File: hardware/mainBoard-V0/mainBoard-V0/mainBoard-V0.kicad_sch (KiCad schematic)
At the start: 20 parts, among them SW1 SW_SPDT, U1 STM32WB55CCU6ND, Y1 ABM12W-32.0MHZ, Y3 ABS07-32.768KHZ

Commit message: Added net labels and assets.
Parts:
- added C15: 4.7u, symbol Device:C
- added E1: AMCA31-2R450G-S1F-T3, AMCA31-2R450G-S1F-T3:XDCR_AMCA31-2R450G-S1F-T3, symbol AMCA31-2R450G-S1F-T3:AMCA31-2R450G-S1F-T3
- added J1: B5B-XH-A, B5B-XH-A:JST_B5B-XH-A, symbol B5B-XH-A:B5B-XH-A
- added L1: 10n, symbol Device:L
- added L2: 10u, symbol Device:L
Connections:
- net GND: now also C15.1
- net SPI1_SCK: now reaches U1.10 (PA1)
- net SPI1_MISO: now reaches U1.15 (PA6)
- net SPI1_MOSI: now reaches U1.16 (PA7)
- net USART1_TX: now reaches U1.18 (PA9)
- net at U1.31 (VFBSMPS): now also C15.2, L2.2
- net at U1.33 (VLXSMPS): now also L1.1
- net USART1_RX: now reaches U1.36 (PA10)
- net USB_DM: now reaches U1.37 (PA11)
- net USB_DP: now reaches U1.38 (PA12)
- new net: L1.2, L2.1
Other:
- moved on the sheet: C5, C6, Y1, Y3

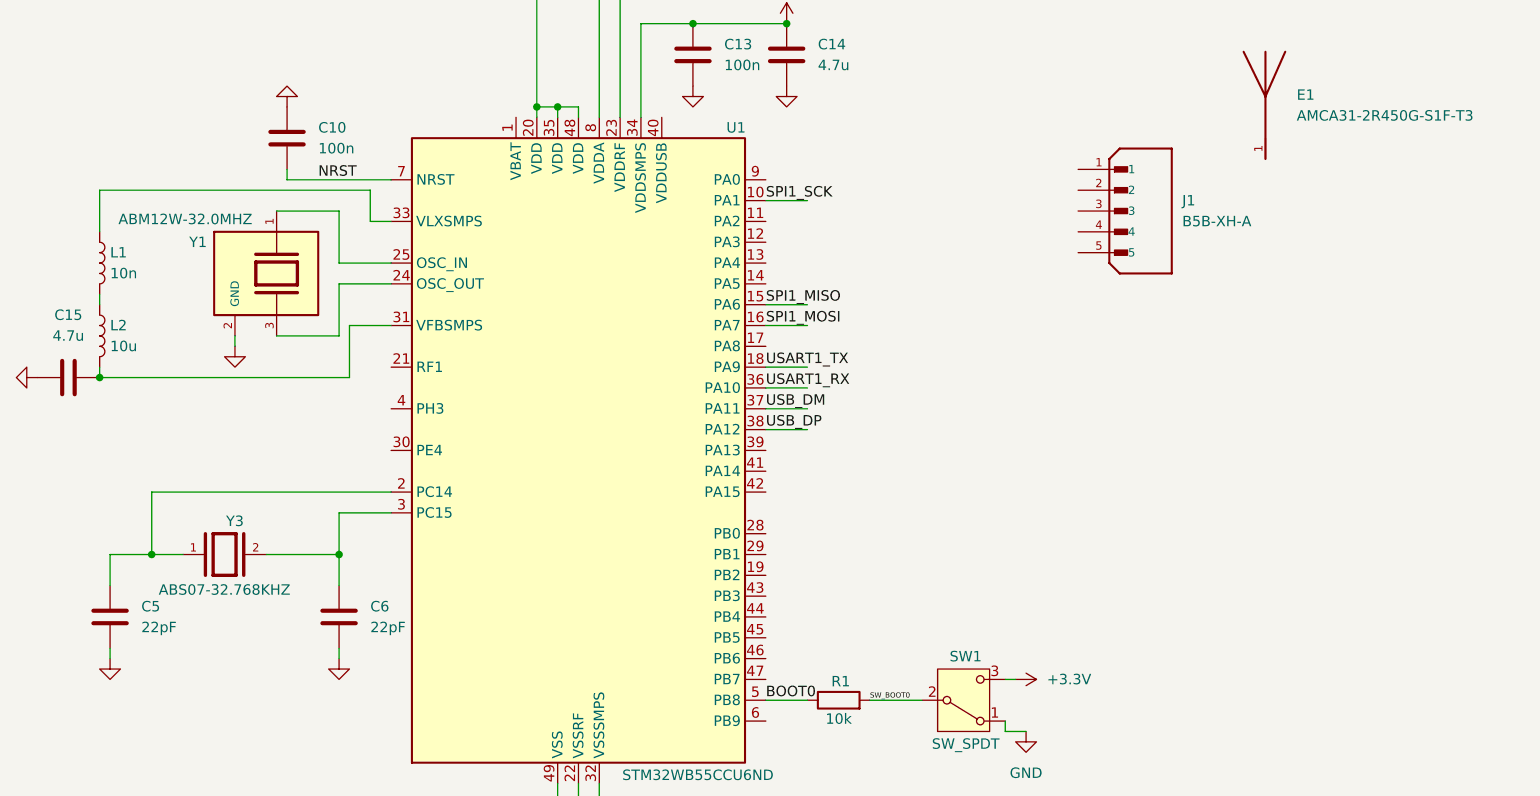
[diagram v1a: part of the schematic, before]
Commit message: Added more components to libraries
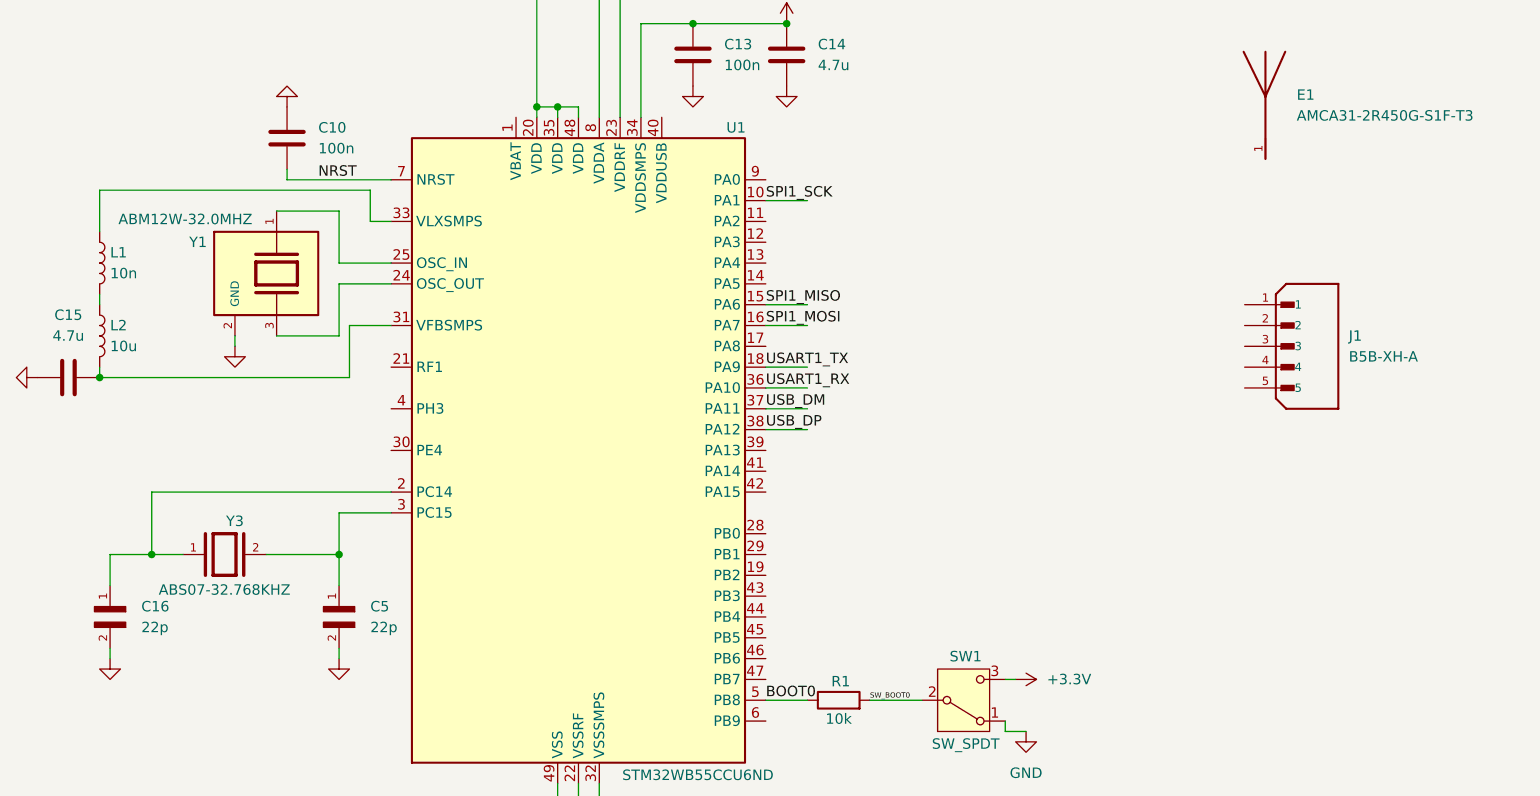
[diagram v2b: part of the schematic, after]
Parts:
- removed C5, C6: 22pF, symbol Device:C
- added C16, C5: 22p, CC0402FRNPO9BN220:CAPC1005X55N, symbol CC0402FRNPO9BN220:CC0402FRNPO9BN220
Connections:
- net GND: now also C16.2, C5.2
- net at U1.3 (PC15), Y3.2: now also C5.1
- net at U1.2 (PC14), Y3.1: now also C16.1
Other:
- moved on the sheet: J1

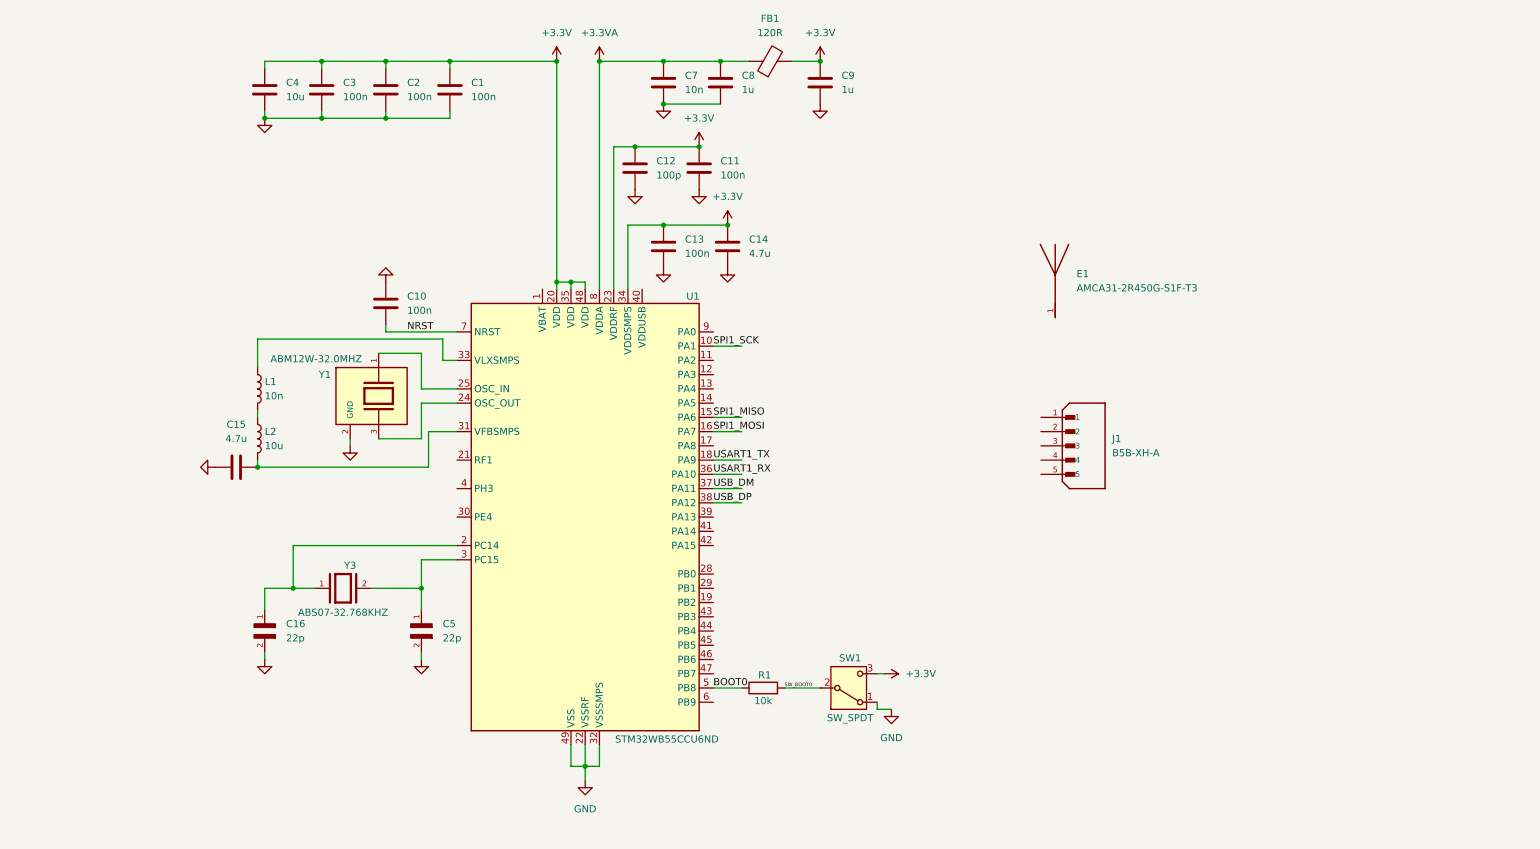
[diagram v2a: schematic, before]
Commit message: Added SWD header, type-c connector, RF antenna circuit, and battery charger with 3v3 regulator for power rail to schematic | Imported real component symbols and datasheets
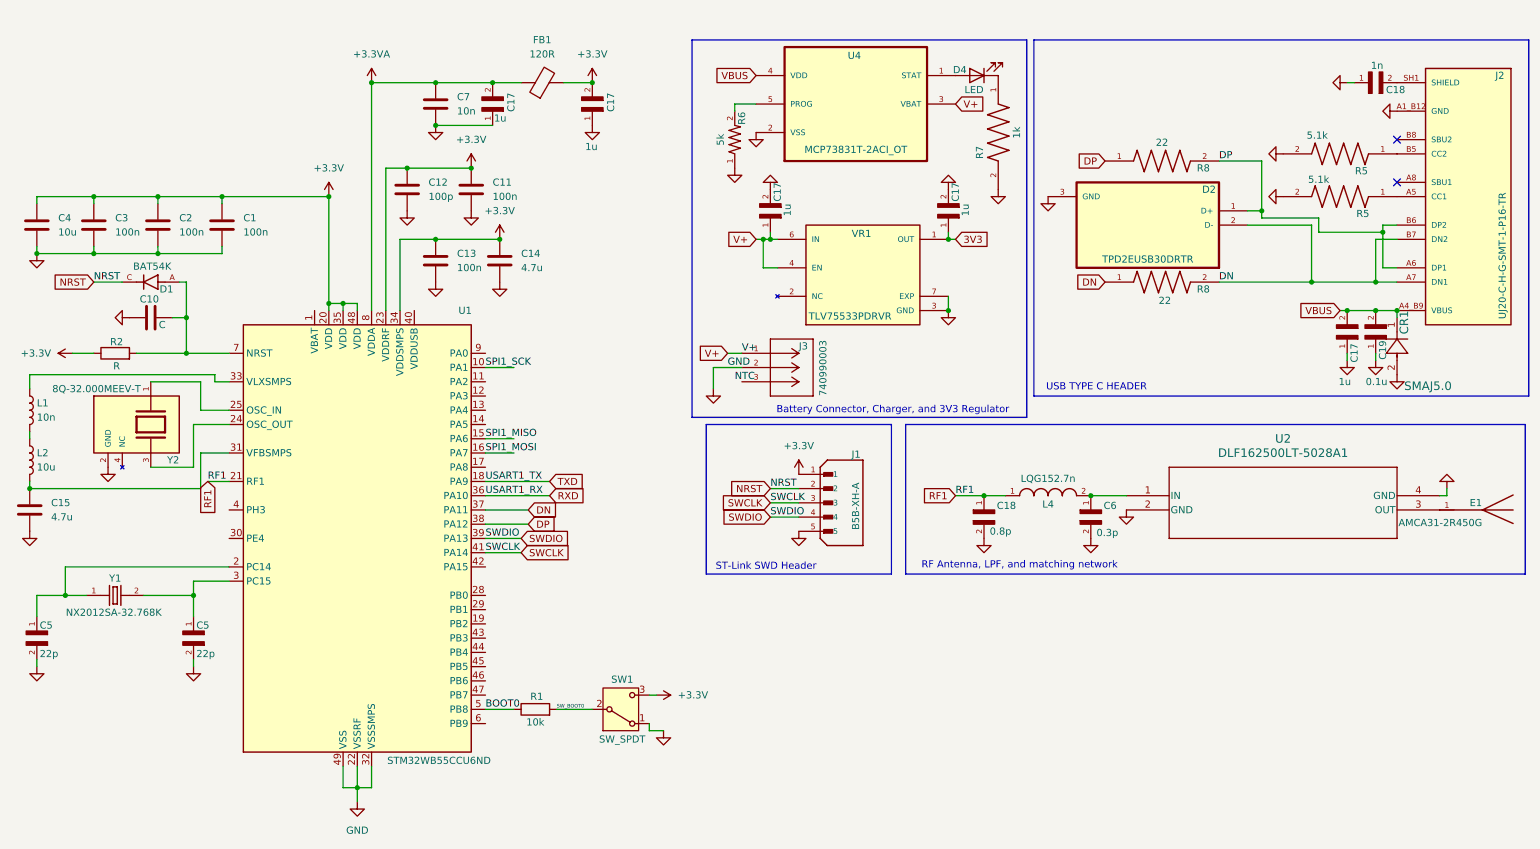
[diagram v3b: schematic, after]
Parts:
- removed C8, C9: 1u, symbol Device:C
- removed Y1: ABM12W-32.0MHZ, ABM12W-32.0000MHZ-6-D1X-T3:XTAL_ABM12W-32.0000MHZ-6-D1X-T3, symbol ABM12W-32.0000MHZ-6-D1X-T3:ABM12W-32.0000MHZ-6-D1X-T3
- removed Y3: ABS07-32.768KHZ, ABS07-32.768KHZ-T:XTAL_ABS07-32.768KHZ-T, symbol ABS07-32.768KHZ-T:ABS07-32.768KHZ-T
- added C17 (x5): 1u, JMK105BJ105KV-F:CAPC1005X55N, symbol JMK105BJ105KV-F:JMK105BJ105KV-F
- added C18: 0.8p, GRM1555C1HR80BA01D:CAPC1005X55N, symbol GRM1555C1HR80BA01D:GRM1555C1HR80BA01D
- added C18: 1n, GRM155R71H102KA01D:CAPC1005X55N, symbol GRM155R71H102KA01D:GRM155R71H102KA01D
- added C19: 0.1u, CL05A104KA5NNNC:CAPC1005X55N, symbol CL05A104KA5NNNC:CL05A104KA5NNNC
- added C6: 0.3p, GRM1555C1HR30WA01D:CAPC1005X55N, symbol GRM1555C1HR30WA01D:GRM1555C1HR30WA01D
- added CR1: SMAJ5.0, SMAJ5-0:SMASeries_LTF, symbol SMAJ5-0:SMAJ5.0
- added D1: BAT54K, BAT54KFILM:SODFL1608X70N, symbol BAT54KFILM:BAT54KFILM
- added D2: TPD2EUSB30DRTR, TPD2EUSB30DRTR:SOTFL35P100X50-3N, symbol TPD2EUSB30DRTR:TPD2EUSB30DRTR
- added D4: LED, symbol Device:LED
- added J2: UJ20-C-H-G-SMT-1-P16-TR, UJ20-C-H-G-SMT-1-P16-TR:SAMESKY_UJ20-C-H-G-SMT-1-P16-TR, symbol UJ20-C-H-G-SMT-1-P16-TR:UJ20-C-H-G-SMT-1-P16-TR
- added J3: 740990003, 740990003:CONN_SD-74099-001_03_MOL, symbol 740990003:740990003
- added L4: LQG152.7n, LQG15HS2N7S02D:INDC1005X55N, symbol LQG15HS2N7S02D:LQG15HS2N7S02D
- added R2: R, symbol Device:R
- added R5 (x2): 5.1k, CRCW04025K10FKED:RESC1005X40N, symbol CRCW04025K10FKED:CRCW04025K10FKED
- added R6: 5k, PNM0402E5001BST1:RESC1005X40, symbol PNM0402E5001BST1:PNM0402E5001BST1
- added R7: 1k, CRCW04021K00FKED:RESC1005X40N, symbol CRCW04021K00FKED:CRCW04021K00FKED
- added R8 (x2): 22, CRCW040222R0FKED:RESC1005X40N, symbol CRCW040222R0FKED:CRCW040222R0FKED
- added U2: DLF162500LT-5028A1, DLF-4_1P6X0P8, symbol 2026-02-12_05-16-45:DLF162500LT-5028A1
- added U4: MCP73831T-2ACI_OT, MCP73831T-2ACI_OT:SOT95P280X145-5N, symbol MCP73831T-2ACI_OT:MCP73831T-2ACI_OT
- added VR1: TLV75533PDRVR, TLV75533PDRVR:VREG_TLV75533PDRVR, symbol TLV75533PDRVR:TLV75533PDRVR
- added Y1: NX2012SA-32.768K, NX2012SA-32.768K-STD-MUB-1:XTAL_NX2012SA-32.768K-STD-MUB-1, symbol NX2012SA-32.768K-STD-MUB-1:NX2012SA-32.768K-STD-MUB-1
- added Y2: 8Q-32.000MEEV-T, 8Q-32.000MEEV-T:XTAL_8Q-32.000MEEV-T, symbol 8Q-32.000MEEV-T:8Q-32.000MEEV-T
- C10: value 100n -> C
- E1: value AMCA31-2R450G-S1F-T3 -> AMCA31-2R450G
- renumbered C16 to C5
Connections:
- net +3.3V: now also J1.1, C17.2, R2.1
- net +3.3VA: now also C17.2
- net GND: now also J1.5, C17.1, C17.1, C17.1, C17.2, C17.2, C18.1, C18.2, C19.1, C6.2, CR1.2, D2.3 (GND), J2.A1_B12 (GND), J2.B1_A12 (GND), J3.2, R5.2, R5.2, R6.1, R7.2, U2.2 (GND), U2.4 (GND), U4.2 (VSS), VR1.3 (GND), VR1.7 (EXP), Y2.2 (GND)
- net NRST: now also J1.2, D1.C; no longer C10.2, U1.7 (NRST)
- net SWCLK: now reaches J1.3
- net SWCLK: now also U1.41 (PA14)
- net SWDIO: now reaches J1.4
- net SWDIO: now also U1.39 (PA13)
- net at C5.1, U1.2 (PC14): now also Y1.1
- net RF1: now reaches U1.21 (RF1)
- net RF1: now also C18.1, L4.1
- net at U1.24 (OSC_OUT): now also Y2.3
- net at U1.25 (OSC_IN): now also Y2.1
- net at C5.1, U1.3 (PC15): now also Y1.2
- net at E1.1: now also U2.3 (OUT)
- net USART1_RX renamed RXD
- net USART1_TX renamed TXD
- net USB_DM renamed DN
- net DN: now also D2.2 (D-), J2.A7 (DN1), J2.B7 (DN2), R8.1, R8.2
- net USB_DP renamed DP
- net DP: now also D2.1 (D+), J2.A6 (DP1), J2.B6 (DP2), R8.1, R8.2
- new net: D4.1 (K), R7.1
- new net: C10.2, D1.A, R2.2, U1.7 (NRST)
- new net: J2.A5 (CC1), R5.1
- new net: C6.1, L4.2, U2.1 (IN)
- new net: C18.2, J2.SH1 (SHIELD), J2.SH2 (SHIELD), J2.SH3 (SHIELD), J2.SH4 (SHIELD)
- new net: J2.B5 (CC2), R5.1
- new net: R6.2, U4.5 (PROG)
- new net: D4.2 (A), U4.1 (STAT)
- new net: VR1.2 (NC), VR1.5 (NC)
- new net 3V3: C17.1, VR1.1 (OUT)
- new net V+: C17.1, J3.1, U4.3 (VBAT), VR1.4 (EN), VR1.6 (IN)
- new net VBUS: C17.2, C19.2, CR1.1, J2.A4_B9 (VBUS), J2.B4_A9 (VBUS), U4.4 (VDD)
- no-connect marks 0 -> 2
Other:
- note added: "Battery Connector, Charger, and 3V3 Regulator"
- note added: "RF Antenna, LPF, and matching network"
- note added: "ST-Link SWD Header"
- note added: "USB TYPE C HEADER"
- moved on the sheet: C1, C11, C12, C13, C14, C15, C2, C3, C4, C5, C7, E1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
